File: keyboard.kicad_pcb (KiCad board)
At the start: 2 copper layers, 398 parts, among them IC1 WS2812B, IC10 WS2812B, IC11 WS2812B, IC12 WS2812B, IC13 WS2812B, IC14 WS2812B, IC15 WS2812B, IC16 WS2812B, IC17 WS2812B, IC18 WS2812B, IC19 WS2812B, IC2 WS2812B, IC20 WS2812B, IC21 WS2812B, IC22 WS2812B, IC23 WS2812B, IC24 WS2812B, IC25 WS2812B, IC26 WS2812B, IC27 WS2812B, IC28 WS2812B, IC29 WS2812B, IC3 WS2812B, IC30 WS2812B, IC31 WS2812B, IC32 WS2812B, IC33 WS2812B, IC34 WS2812B, IC35 WS2812B, IC36 WS2812B, IC37 WS2812B, IC38 WS2812B, IC39 WS2812B, IC4 WS2812B, IC40 WS2812B, IC41 WS2812B, IC42 WS2812B, IC43 WS2812B, IC44 WS2812B, IC45 WS2812B, IC46 WS2812B, IC47 WS2812B, IC48 WS2812B, IC49 WS2812B, IC5 WS2812B, IC50 WS2812B, IC51 WS2812B, IC52 WS2812B, IC53 WS2812B, IC54 WS2812B, IC55 WS2812B, IC56 WS2812B, IC57 WS2812B, IC58 WS2812B, IC59 WS2812B, IC6 WS2812B, IC60 WS2812B, IC61 WS2812B, IC62 WS2812B, IC63 WS2812B, IC64 WS2812B, IC65 WS2812B, IC66 WS2812B, IC67 WS2812B, IC68 WS2812B, IC69 WS2812B, IC7 WS2812B, IC70 WS2812B, IC71 WS2812B, IC72 WS2812B, IC73 WS2812B, IC74 WS2812B, IC75 WS2812B, IC76 WS2812B, IC77 WS2812B, IC78 WS2812B, IC79 WS2812B, IC8 WS2812B, IC80 WS2812B, IC81 WS2812B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

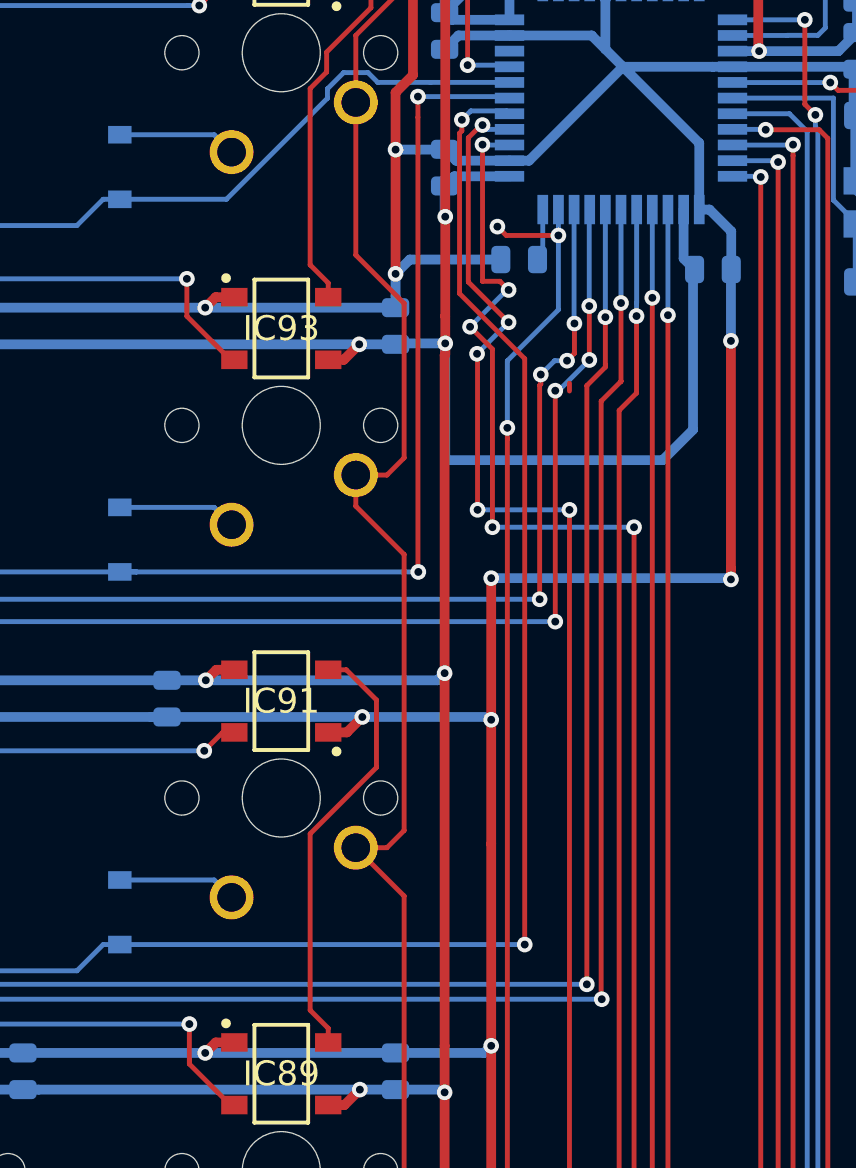
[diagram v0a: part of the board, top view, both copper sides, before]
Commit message: Track Routing Cleaning
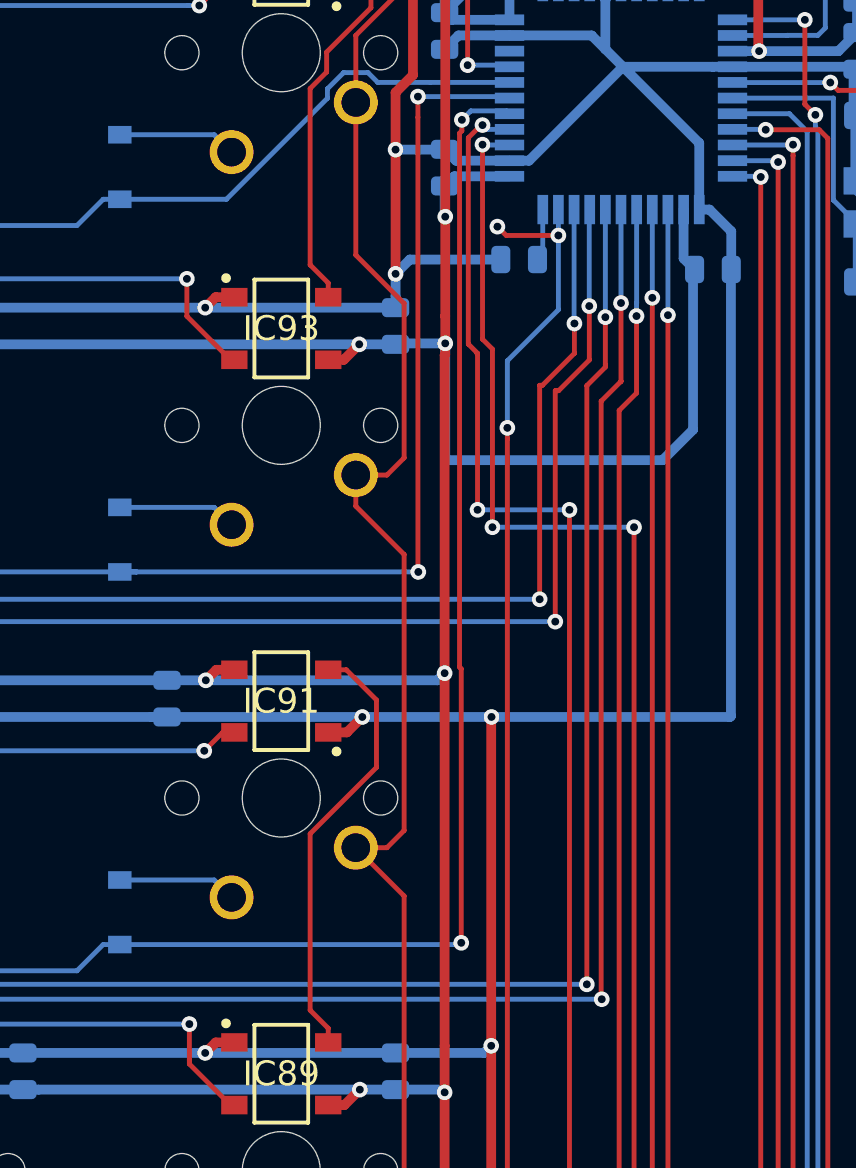
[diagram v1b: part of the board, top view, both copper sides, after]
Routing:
- net ROW3: track 393.1 -> 388.3 mm
- net ROW5: track 446.6 -> 444.4 mm, vias 6 -> 4
- net ROW4: track 420.1 -> 418.4 mm, vias 6 -> 4
- net GND: track 2425.2 -> 2424.9 mm, vias 107 -> 104
- net COL7: track 303.4 -> 303.1 mm, vias 5 -> 3
- net COL8: vias 5 -> 3

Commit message: Track Routine Cleaning
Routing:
- net +5V: track 2356.3 -> 2344.5 mm
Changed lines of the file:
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@@
     (thickness 1.6)
     (drawings 13)
-    (tracks 3227)
+    (tracks 3223)
     (zones 0)
     (modules 398)
@@
   )
   (setup
-    (last_trace_width 0.25)
+    (last_trace_width 0.5)
     (user_trace_width 0.25)
     (user_trace_width 0.4)
@@
   (segment (start 316.738 -64.712315) (end 316.70625 -64.680565) (width 0.5) (layer F.Cu) (net 2))
   (segment (start 316.738 -65.278) (end 316.738 -64.712315) (width 0.5) (layer F.Cu) (net 2))
-  (segment (start 316.738 -59.309) (end 316.738 -65.278) (width 0.5) (layer B.Cu) (net 2))
-  (segment (start 327.8505 -59.309) (end 316.738 -59.309) (width 0.5) (layer B.Cu) (net 2))
-  (segment (start 329.40625 -60.86475) (end 327.8505 -59.309) (width 0.5) (layer B.Cu) (net 2))
   (segment (start 329.48475 -69.05625) (end 329.40625 -68.97775) (width 0.5) (layer B.Cu) (net 2))
-  (segment (start 329.40625 -68.97775) (end 329.40625 -60.86475) (width 0.5) (layer B.Cu) (net 2))
+  (segment (start 317.303685 -65.278) (end 316.738 -65.278) (width 0.5) (layer B.Cu) (net 2))
+  (segment (start 327.939502 -65.278) (end 317.303685 -65.278) (width 0.5) (layer B.Cu) (net 2))
+  (segment (start 329.48475 -66.823248) (end 327.939502 -65.278) (width 0.5) (layer B.Cu) (net 2))
+  (segment (start 329.48475 -69.05625) (end 329.48475 -66.823248) (width 0.5) (layer B.Cu) (net 2))
   (segment (start 337.70025 -68.50875) (end 337.61275 -68.42125) (width 0.25) (layer B.Cu) (net 3))
   (segment (start 337.70025 -71.38525) (end 337.70025 -68.50875) (width 0.25) (layer B.Cu) (net 3))
@@
   (segment (start 118.49449 -39.497) (end 119.373501 -40.376011) (width 0.25) (layer F.Cu) (net 114))
   (segment (start 116.9035 -39.497) (end 118.49449 -39.497) (width 0.25) (layer F.Cu) (net 114))
-  (via (at 319.913 -60.96) (size 0.8) (drill 0.4) (layers F.Cu B.Cu) (net 114))
-  (segment (start 322.52325 -66.99925) (end 319.913 -64.389) (width 0.25) (layer B.Cu) (net 114))
-  (segment (start 319.913 -64.389) (end 319.913 -60.96) (width 0.25) (layer B.Cu) (net 114))
   (via (at 322.52325 -70.79575) (size 0.8) (drill 0.4) (layers F.Cu B.Cu) (net 114))
   (segment (start 322.52325 -70.92275) (end 322.52325 -70.79575) (width 0.25) (layer B.Cu) (net 114))
@@
   (segment (start 200.246099 -14.510901) (end 202.184 -12.573) (width 0.25) (layer B.Cu) (net 114))
   (segment (start 202.184 -12.573) (end 315.361001 -12.573) (width 0.25) (layer B.Cu) (net 114))
-  (segment (start 315.361001 -12.573) (end 317.774001 -10.16) (width 0.25) (layer F.Cu) (net 114))
-  (segment (start 319.913 -60.394315) (end 319.913 -60.96) (width 0.25) (layer F.Cu) (net 114))
-  (segment (start 319.913 -11.658748) (end 319.913 -60.394315) (width 0.25) (layer F.Cu) (net 114))
+  (via (at 322.52325 -66.99925) (size 0.8) (drill 0.4) (layers F.Cu B.Cu) (net 114))
+  (segment (start 319.913 -64.389) (end 322.52325 -66.99925) (width 0.25) (layer F.Cu) (net 114))
+  (segment (start 319.913 -11.658748) (end 319.913 -64.389) (width 0.25) (layer F.Cu) (net 114))
   (segment (start 318.414252 -10.16) (end 319.913 -11.658748) (width 0.25) (layer F.Cu) (net 114))
+  (segment (start 315.361001 -12.573) (end 317.774001 -10.16) (width 0.25) (layer F.Cu) (net 114))
   (segment (start 317.774001 -10.16) (end 318.414252 -10.16) (width 0.25) (layer F.Cu) (net 114))
   (segment (start 123.25699 -77.597) (end 121.666 -77.597) (width 0.25) (layer F.Cu) (net 115))
@@
   (segment (start 286.89159 -52.197) (end 287.755501 -53.060911) (width 0.25) (layer B.Cu) (net 115))
   (segment (start 287.755501 -53.060911) (end 290.8565 -53.06091) (width 0.25) (layer B.Cu) (net 115))
-  (segment (start 321.564 -52.197) (end 321.564 -63.134349) (width 0.25) (layer F.Cu) (net 115))
-  (segment (start 321.706349 -63.134349) (end 323.342 -64.77) (width 0.25) (layer F.Cu) (net 115))
-  (segment (start 321.564 -63.134349) (end 321.706349 -63.134349) (width 0.25) (layer F.Cu) (net 115))
+  (segment (start 321.564 -62.992) (end 323.342 -64.77) (width 0.25) (layer F.Cu) (net 115))
+  (segment (start 321.564 -52.197) (end 321.564 -62.992) (width 0.25) (layer F.Cu) (net 115))
   (segment (start 142.30699 -77.597) (end 140.716 -77.597) (width 0.25) (layer F.Cu) (net 116))
   (segment (start 143.186001 -78.476011) (end 142.30699 -77.597) (width 0.25) (layer F.Cu) (net 116))
@@
   (via (at 322.363 -51.054) (size 0.8) (drill 0.4) (layers F.Cu B.Cu) (net 116))
   (segment (start 292.227 -51.054) (end 322.363 -51.054) (width 0.25) (layer B.Cu) (net 116))
-  (segment (start 322.363 -51.054) (end 322.363 -62.860347) (width 0.25) (layer F.Cu) (net 116))
   (via (at 324.100153 -67.185654) (size 0.8) (drill 0.4) (layers F.Cu B.Cu) (net 116))
-  (segment (start 324.104 -64.428) (end 324.104 -67.181807) (width 0.25) (layer F.Cu) (net 116))
-  (segment (start 324.104 -67.181807) (end 324.100153 -67.185654) (width 0.25) (layer F.Cu) (net 116))
   (segment (start 324.100153 -72.096153) (end 324.12325 -72.11925) (width 0.25) (layer B.Cu) (net 116))
   (segment (start 324.100153 -67.185654) (end 324.100153 -72.096153) (width 0.25) (layer B.Cu) (net 116))
-  (segment (start 322.536347 -62.860347) (end 324.104 -64.428) (width 0.25) (layer F.Cu) (net 116))
-  (segment (start 322.363 -62.860347) (end 322.536347 -62.860347) (width 0.25) (layer F.Cu) (net 116))
+  (segment (start 324.104 -64.428) (end 324.104 -67.181807) (width 0.25) (layer F.Cu) (net 116))
+  (segment (start 324.104 -67.181807) (end 324.100153 -67.185654) (width 0.25) (layer F.Cu) (net 116))
+  (segment (start 322.363 -62.687) (end 322.363 -51.054) (width 0.25) (layer F.Cu) (net 116))
+  (segment (start 324.104 -64.428) (end 322.363 -62.687) (width 0.25) (layer F.Cu) (net 116))
   (segment (start 161.35699 -77.597) (end 159.766 -77.597) (width 0.25) (layer F.Cu) (net 117))
   (segment (start 162.236001 -78.476011) (end 161.35699 -77.597) (width 0.25) (layer F.Cu) (net 117))

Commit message: Ground Fill, Track Clearances, USB C CC & VCONN
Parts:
- added R7: 5.1k, Resistor_SMD:R_0805_2012Metric, B.Cu at (325.1, -99.8)
- added R8: 5.1k, Resistor_SMD:R_0805_2012Metric, F.Cu at (328.4, -100.7)
- moved C3 6.22 mm to (338.4, -62.2)
- moved C4 6.22 mm to (338.4, -70.7)
- moved Y1 6.22 mm to (338.4, -66.3)
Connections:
- P1 pad A8: (no net) -> Net-(P1-PadA8)
- P1 pad B6: (no net) -> D+
- P1 pad B7: (no net) -> D-
- P1 pad B8: (no net) -> Net-(P1-PadB8)
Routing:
- net Net-(P1-PadB5): track 0.00 -> 11.5 mm
- net GND: track 2424.9 -> 2435.8 mm, vias 104 -> 105
- net Net-(C4-Pad1): track 13.9 -> 19.7 mm
- net Net-(C3-Pad1): track 15.1 -> 20.9 mm
- net +5V: track 2344.5 -> 2350.2 mm
- net COL2: track 514.4 -> 516.6 mm
- net COL1: track 537.3 -> 539.5 mm
- net D-: track 10.2 -> 12.1 mm
- net Net-(P1-PadA5): track 0.00 -> 1.76 mm
- net D+: track 10.2 -> 11.9 mm
- net COL3: track 495.0 -> 496.0 mm
- net COL4: track 464.0 -> 464.8 mm
- net COL0: track 555.8 -> 556.5 mm
- added copper zone on B.Cu, net GND

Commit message: Edge Cut, Mounting Holes, Silk Screen
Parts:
- added REF**: MountingHole_4.3mm_M4, MountingHole:MountingHole_4.3mm_M4, F.Cu at (118.8, -2.94)
- added REF**: MountingHole_4.3mm_M4, MountingHole:MountingHole_4.3mm_M4, F.Cu at (336.6, -104.0)
- added REF**: MountingHole_4.3mm_M4, MountingHole:MountingHole_4.3mm_M4, F.Cu at (178.8, -2.94)
- added REF**: MountingHole_4.3mm_M4, MountingHole:MountingHole_4.3mm_M4, F.Cu at (104.0, -113.5)
- added REF**: MountingHole_4.3mm_M4, MountingHole:MountingHole_4.3mm_M4, F.Cu at (188.9, -113.5)
- added REF**: MountingHole_4.3mm_M4, MountingHole:MountingHole_4.3mm_M4, F.Cu at (303.2, -113.5)
- added REF**: MountingHole_4.3mm_M4, MountingHole:MountingHole_4.3mm_M4, F.Cu at (-20.6, -113.5)
- added REF**: MountingHole_4.3mm_M4, MountingHole:MountingHole_4.3mm_M4, F.Cu at (-30.2, 1.59)
- added REF**: MountingHole_4.3mm_M4, MountingHole:MountingHole_4.3mm_M4, F.Cu at (-30.2, -104.0)
- added REF**: MountingHole_4.3mm_M4, MountingHole:MountingHole_4.3mm_M4, F.Cu at (336.6, 1.59)
- R8: moved to B.Cu
- moved R8 0.25 mm to (328.2, -100.7)
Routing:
- net COL0: track 556.5 -> 544.9 mm
- net COL1: track 539.5 -> 532.6 mm
- net Net-(IC30-Pad2): track 72.7 -> 74.1 mm
- net Net-(IC36-Pad2): track 70.2 -> 71.5 mm
- net COL3: track 496.0 -> 494.8 mm
- net +5V: track 2350.2 -> 2351.2 mm
- net COL2: track 516.6 -> 516.0 mm
- net GND: track 2435.8 -> 2435.4 mm, vias 105 -> 104
- net Net-(P1-PadB5): track 11.5 -> 11.6 mm, vias 0 -> 1
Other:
- board outline added: 376.2 x 124.6 mm
- board text added: "Rishaan.nz"

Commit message: Production
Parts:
- moved SW1 51.0 mm to (325.4, -40.6), turned to 0 degrees
- moved R4 48.7 mm to (319.0, -38.7), turned to 0 degrees
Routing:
- net Net-(R4-Pad2): track 11.7 -> 71.7 mm
- net GND: track 2435.4 -> 2440.3 mm
- net +5V: track 2351.2 -> 2352.6 mm, vias 106 -> 107
- net COL2: track 516.0 -> 516.2 mm, vias 0 -> 2
- net COL1: vias 4 -> 6
